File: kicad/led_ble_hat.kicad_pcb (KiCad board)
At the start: 4 copper layers, 35 x 35 mm, 73 parts, among them J1 USB_C_Receptacle_USB2.0_14P, J2 Battery, J3 Prog, J4 DEBUG, J5 Strip, Q1 2N7002, Q2 AO3401A, Q3 2N7002, Q4 AO3401A, Q5 2N7002, Q6 2N7002, Q7 BSS84, Q8 BSS84, SW1 SW_Reed, U1 TP4054, U2 XC6206P332MR, U3 STM32WB55CGUx, Y1 32Mhz

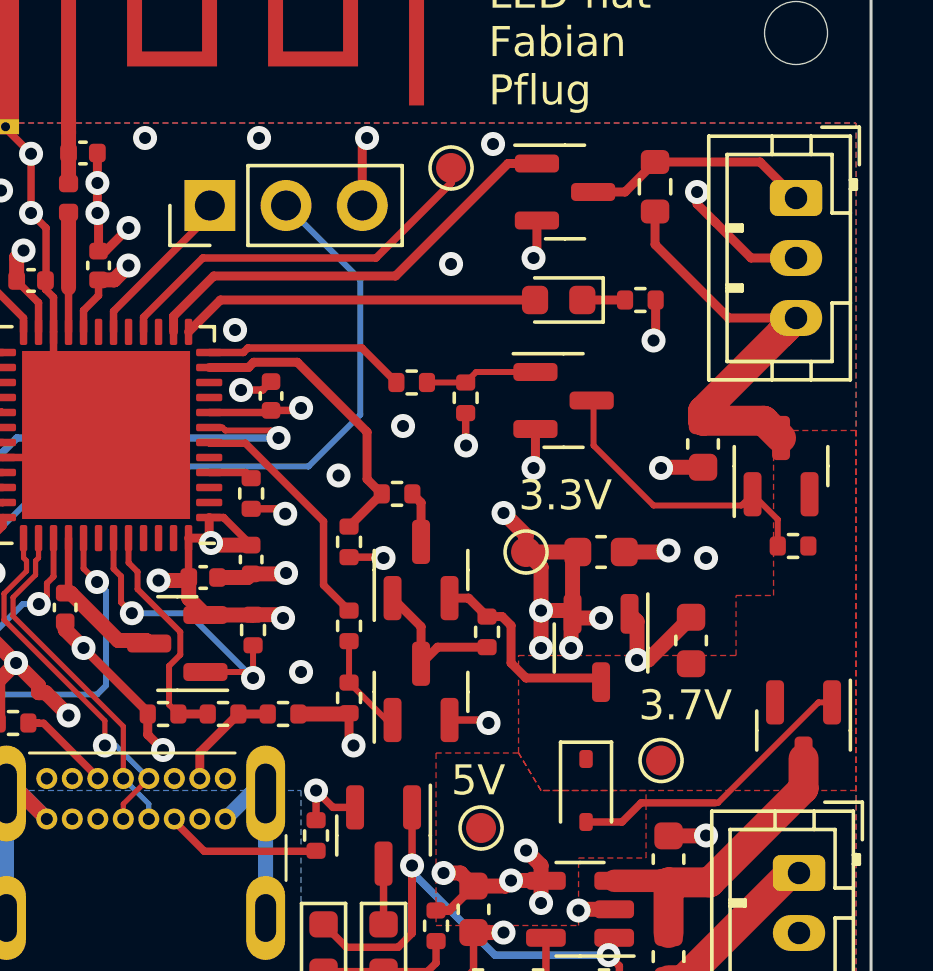
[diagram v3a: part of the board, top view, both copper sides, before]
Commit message: Add descriptions for connectors
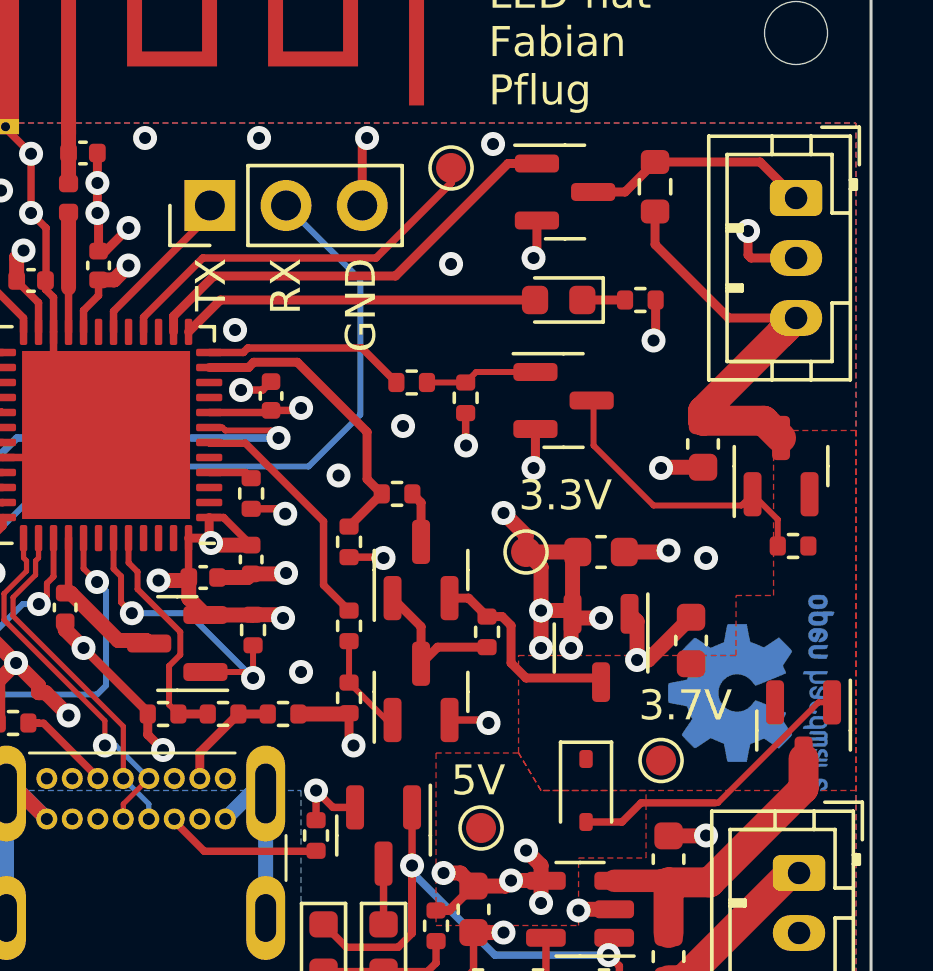
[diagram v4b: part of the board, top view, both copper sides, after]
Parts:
- added REF**: OSHW-Logo2_7.3x6mm_Copper, Symbol:OSHW-Logo2_7.3x6mm_Copper, B.Cu at (161.0, 59.5)
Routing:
- net GND: track 114.5 -> 112.5 mm
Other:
- board text added: "+"
- board text added: "-"
- board text added: "BATT+"
- board text added: "DATA"
- board text added: "GND"
- board text added: "RX"
- board text added: "TX"
- board text added: "VCC"

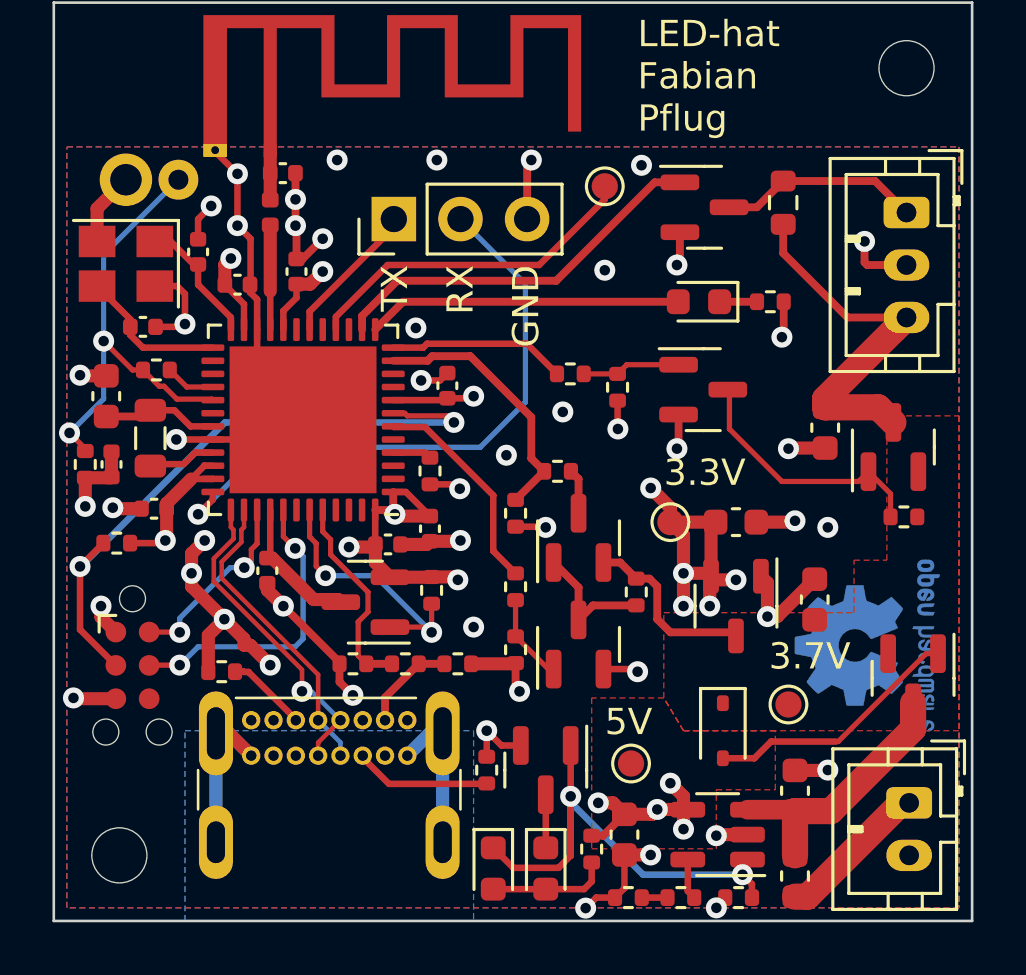
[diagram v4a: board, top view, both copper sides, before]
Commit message: Update to Kicad 8
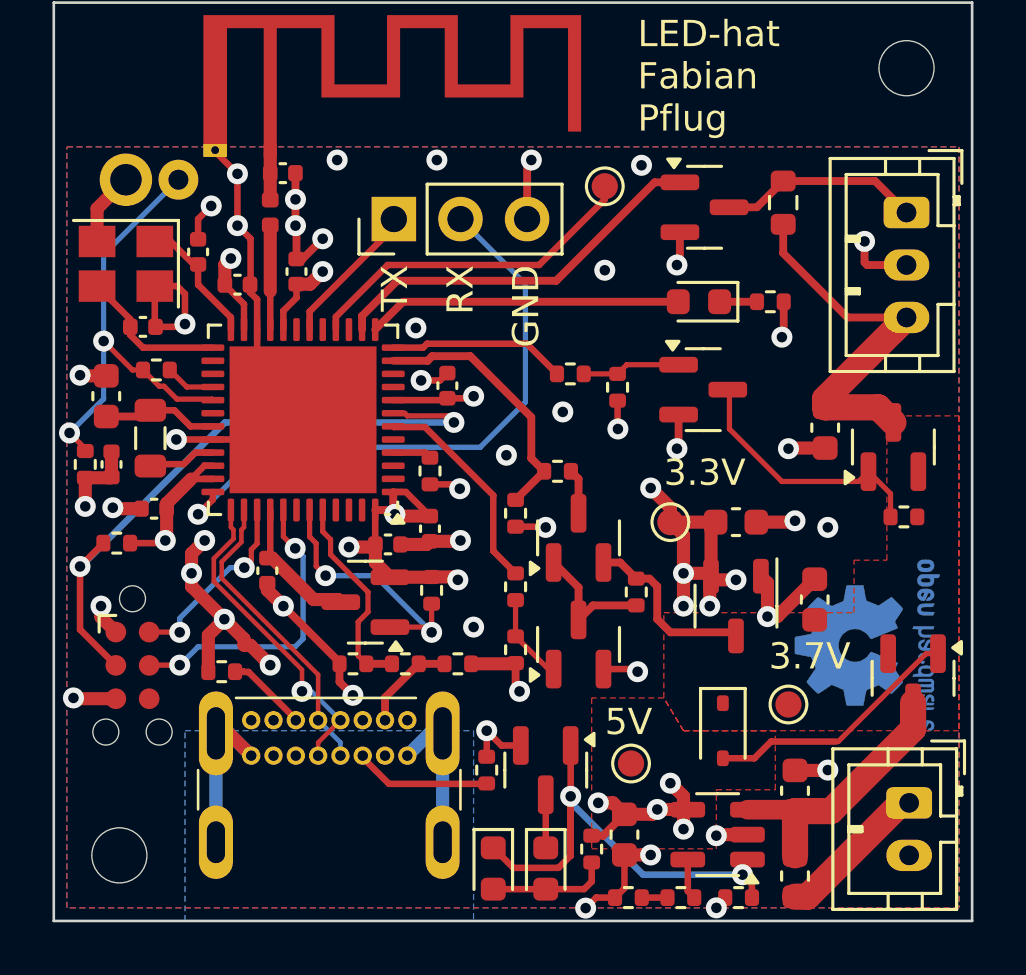
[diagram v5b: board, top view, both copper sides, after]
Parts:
- SW1: value SW_Reed -> SW-18010P
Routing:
- net GND: track 112.5 -> 114.1 mm

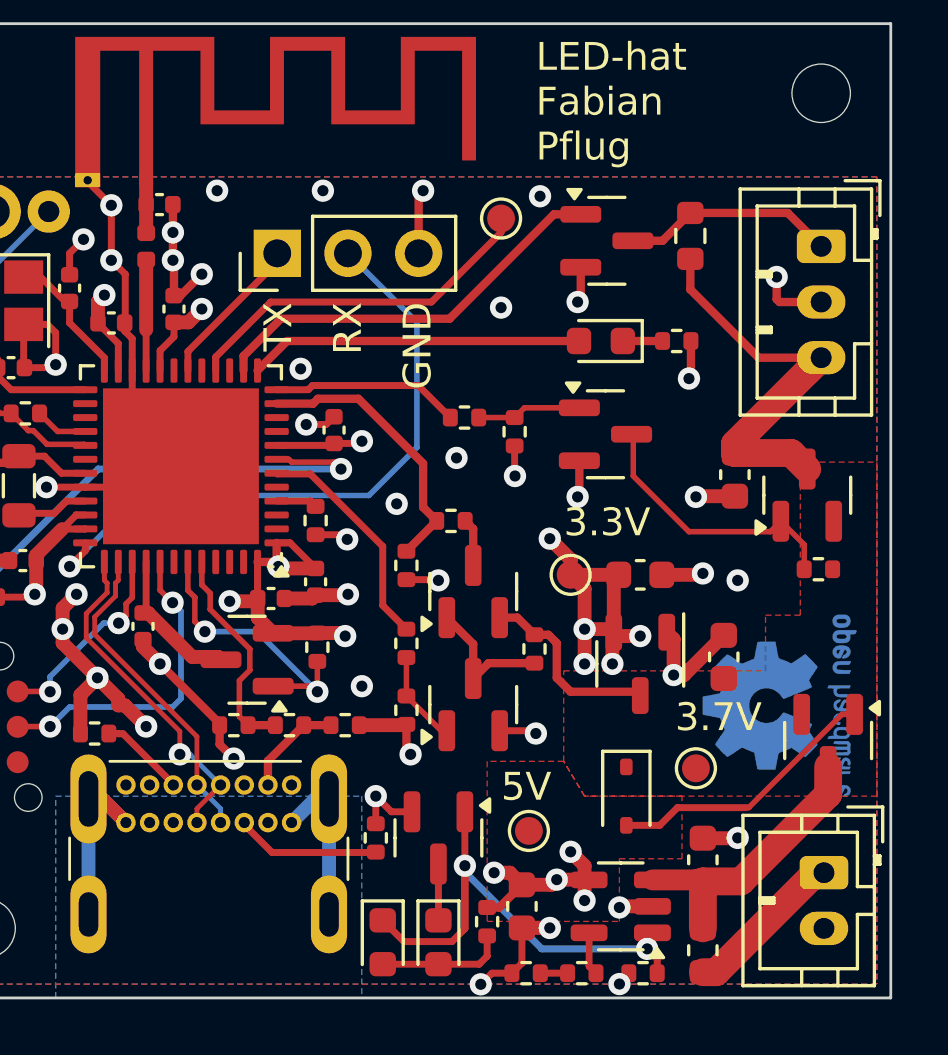
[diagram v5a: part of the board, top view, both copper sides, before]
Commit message: Add double inverter for ws2812b output
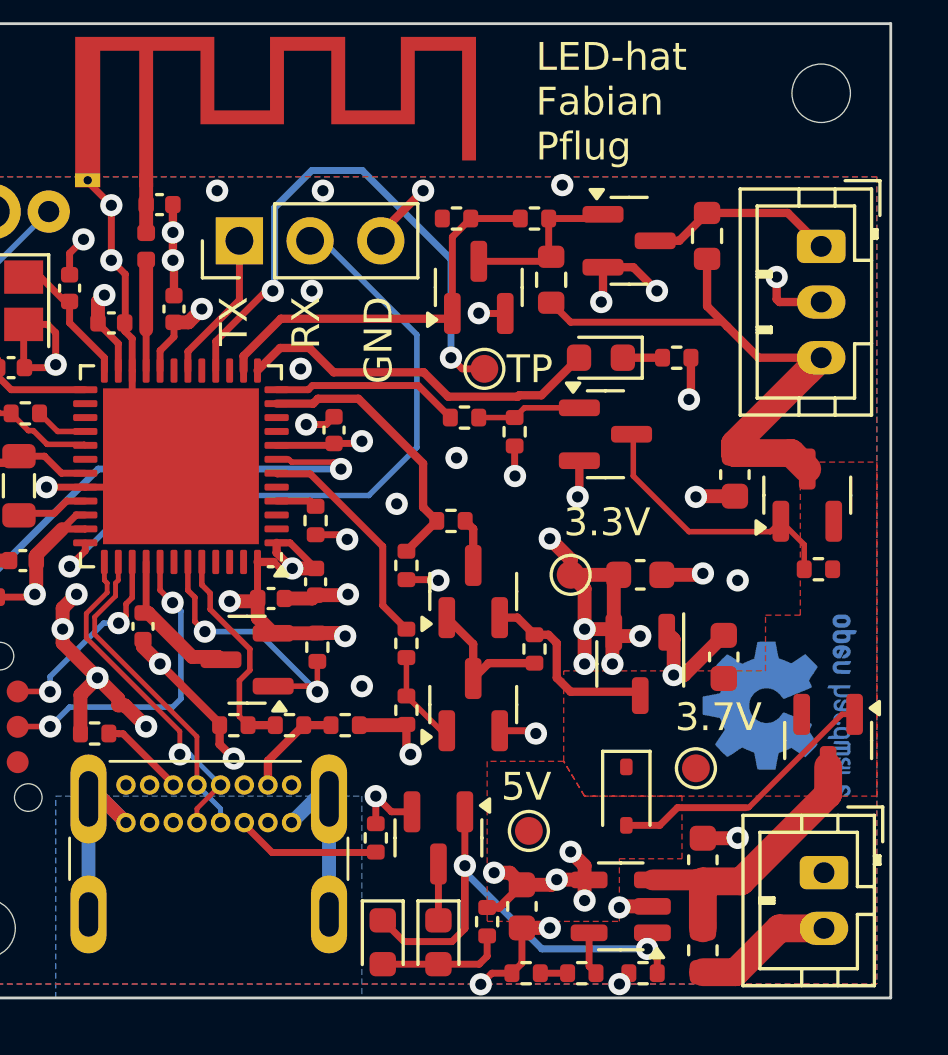
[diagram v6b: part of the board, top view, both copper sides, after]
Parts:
- added Q101: 2N7002, Package_TO_SOT_SMD:SOT-23, F.Cu at (150.2, 44.5)
- added R101: 100k, Resistor_SMD:R_0402_1005Metric, F.Cu at (149.4, 42.0)
- added R102: 1k, Resistor_SMD:R_0603_1608Metric, F.Cu at (152.8, 44.2)
- added R103: 0R, Resistor_SMD:R_0402_1005Metric, F.Cu at (152.2, 42.0)
- J1: footprint led-hat:GSB1C211110DS1HR -> g-Connector_USB:GSB1C211110DS1HR
- SW1: footprint led-hat:SW-18010P -> g-Sensor_Motion:SW-18010P_Vertical
- moved TP10 5.43 mm to (150.4, 47.4)
- moved J4 1.43 mm to (141.6, 42.8)
- moved Q5 0.80 mm to (155.6, 42.8)
- moved D5 0.60 mm to (154.6, 47.0)
- moved R18 0.60 mm to (157.3, 47.0)
- moved R14 0.60 mm to (158.4, 42.6)
- turned R3 to 180 degrees
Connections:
- F1 pad 2: Net-(J2-Pin_1) -> Net-(J2-Pin_2)
- J2 pad 1: Net-(J2-Pin_1) -> GND
- J2 pad 2: GND -> Net-(J2-Pin_2)
- Q5 pad 1: WS2812B_3V3 -> Net-(Q101-D)
- R3 pad 1: STRIP_ENABLE -> Net-(Q3-G)
- R3 pad 2: Net-(Q3-G) -> STRIP_ENABLE
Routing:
- net SPI_MOSI: track 13.1 -> 20.0 mm, vias 0 -> 2
- net /STRIP_VDD: track 15.1 -> 21.5 mm
- net Net-(Q101-D): track 0.00 -> 6.09 mm
- net Net-(J2-Pin_1): track 5.83 -> 0.00 mm
- net Net-(J2-Pin_2): track 0.00 -> 5.00 mm
- net GND: track 114.1 -> 116.6 mm, vias 46 -> 47
- net RX: track 23.3 -> 24.6 mm
- net LED_INDICATOR: track 12.0 -> 13.2 mm
- net WS2812B_3V3: track 14.7 -> 13.9 mm
- net /WS2812B_5V: track 7.67 -> 6.87 mm
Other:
- board text added: "TP"

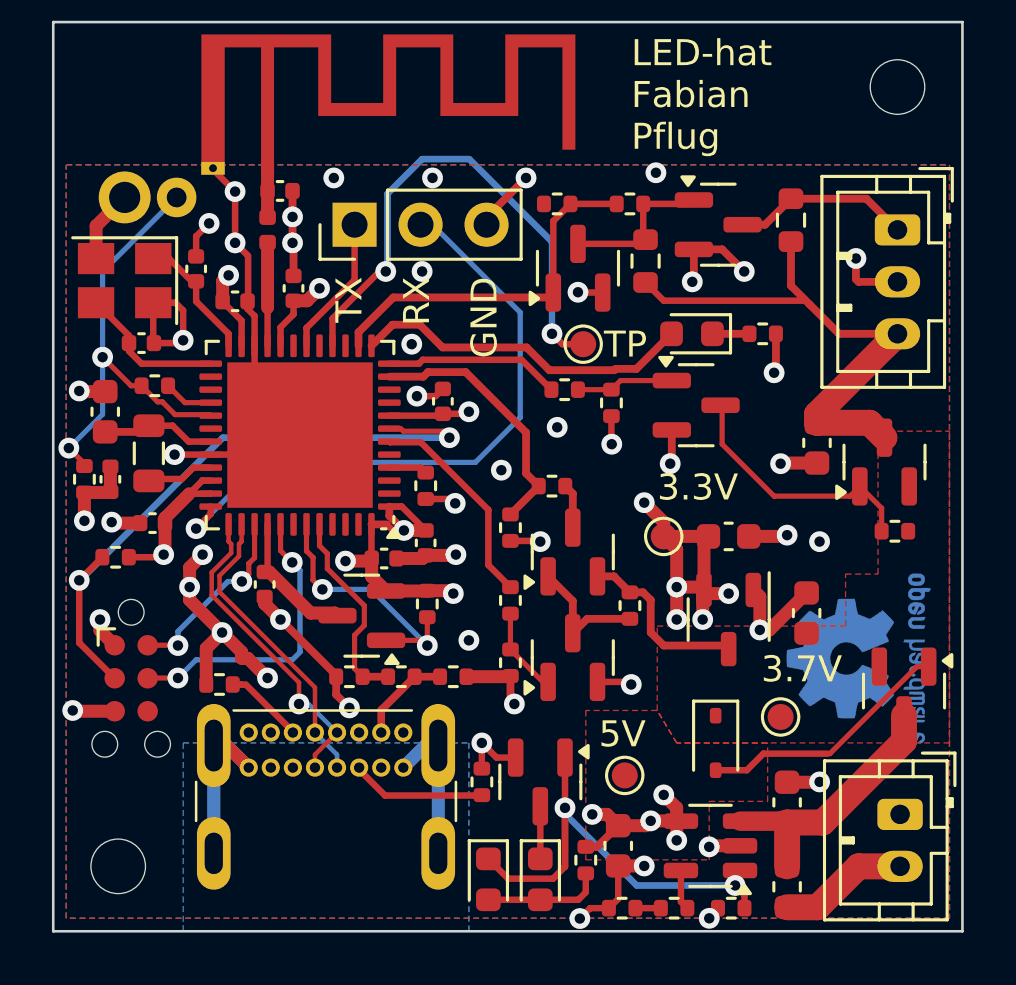
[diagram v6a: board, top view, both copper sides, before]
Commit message: Add accelerometer
Add an accellerometer and gyroscope to maybe add animations and energy
savings based on its output.
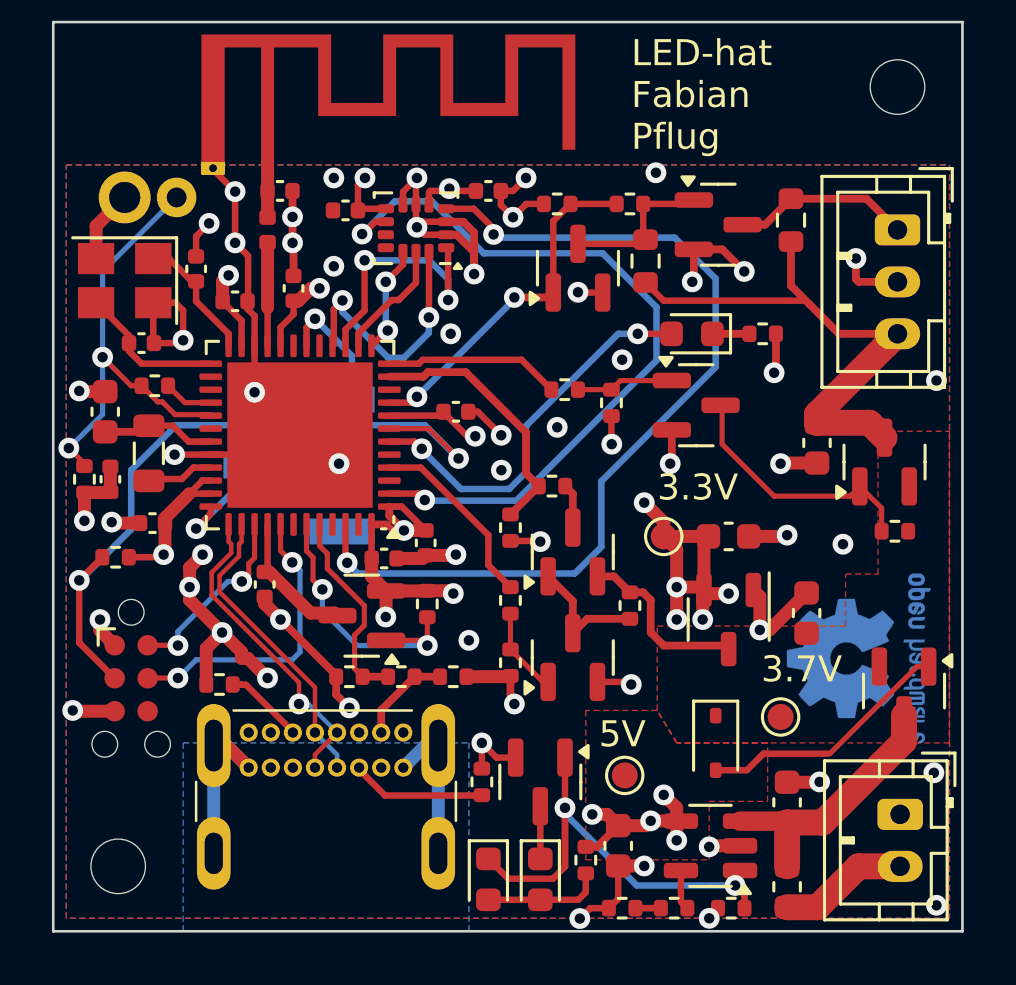
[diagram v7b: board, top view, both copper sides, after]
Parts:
- removed R21: 10k, Resistor_SMD:R_0402_1005Metric
- removed TP10: TestPoint, TestPoint:TestPoint_Pad_D1.0mm
- added C19: 100nF, Capacitor_SMD:C_0402_1005Metric, F.Cu at (146.8, 41.5)
- added C2: 100nF, Capacitor_SMD:C_0402_1005Metric, F.Cu at (141.2, 42.2)
- added U4: LSM6DS3, Package_LGA:LGA-14_3x2.5mm_P0.5mm_LayoutBorder3x4y, F.Cu at (144.0, 42.9)
- J4: footprint Connector_PinHeader_2.54mm:PinHeader_1x03_P2.54mm_Vertical -> Connector_PinHeader_2.54mm:PinHeader_1x03_P2.54mm_Vertical_SMD_Pin1Left; moved to B.Cu
- moved J4 9.51 mm to (139.5, 52.1), turned to 180 degrees
- moved C15 0.64 mm to (145.5, 50.0), turned to 0 degrees
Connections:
- U3 pad 13: LED_INDICATOR -> ACC_CS
- U3 pad 14: WS2812B_3V3 -> ACC_SCK
- U3 pad 15: unconnected-(U3-PA6-Pad15) -> ACC_MISO
- U3 pad 16: SPI_MOSI -> ACC_MOSI
- U3 pad 2: unconnected-(U3-PC14-Pad2) -> ACC_INT2
- U3 pad 4: /Boot0 -> ADC_BAT_EN
- U3 pad 46: unconnected-(U3-PB6-Pad46) -> ACC_INT1
- U3 pad 6: ADC_BAT_EN -> LED_INDICATOR
- U3 pad 9: unconnected-(U3-PA0-Pad9) -> WS2812B_3V3
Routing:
- net ACC_INT1: track 0.00 -> 35.6 mm, vias 0 -> 2
- net ACC_INT2: track 0.00 -> 29.3 mm, vias 0 -> 2
- net RX: track 24.6 -> 4.47 mm
- net SPI_MOSI: track 20.0 -> 0.00 mm, vias 2 -> 0
- net GND: track 116.6 -> 128.0 mm, vias 47 -> 55
- net ACC_MISO: track 0.00 -> 9.96 mm, vias 0 -> 2
- net ACC_MOSI: track 0.00 -> 9.92 mm, vias 0 -> 2
- net +3.3V: track 43.4 -> 48.8 mm, vias 14 -> 16
- net ACC_SCK: track 0.00 -> 4.69 mm
- net ACC_CS: track 0.00 -> 4.20 mm, vias 0 -> 2
- net RESET_N: track 24.6 -> 27.7 mm
- net LED_INDICATOR: track 13.2 -> 15.2 mm, vias 0 -> 2
- net /Boot0: track 1.48 -> 0.00 mm
- net ADC_BAT_EN: track 8.23 -> 7.24 mm
- net WS2812B_3V3: track 13.9 -> 13.4 mm, vias 0 -> 2
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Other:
- board text removed: "TP"

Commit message: Some final touches
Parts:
- added REF**: JLCPCB_Mounting_hole, g-Misc:JLCPCB_Mounting_hole, F.Cu at (158.5, 39.0)
- added REF**: JLCPCB_Mounting_hole, g-Misc:JLCPCB_Mounting_hole, F.Cu at (140.5, 67.0)
- added REF**: JLCPCB_Mounting_hole, g-Misc:JLCPCB_Mounting_hole, F.Cu at (133.0, 39.0)
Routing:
- net GND: track 128.0 -> 124.4 mm, vias 55 -> 56
